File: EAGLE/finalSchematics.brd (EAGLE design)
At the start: 100 x 80 mm, 34 parts, among them IC1 STM32F103RBT, J2 U.FL, J3 U.FL, Q1 8MHz 131-220, U1 LM1117-3.3

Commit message: Death is near
Routing the board
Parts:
- added R1: 10k 901-655, rcl:R0805
- moved JP1 170.6 mm to (38.8, 4.67), flipped to the bottom, turned to 340 degrees
- moved LED3 167.3 mm to (49.5, 29.8), turned to 270 degrees
- moved 270OHM2 166.9 mm to (45.2, 29.8), turned to 180 degrees
- moved 270OHM1 158.5 mm to (45.2, 27.6), turned to 180 degrees
- moved LED2 158.3 mm to (49.5, 27.4), turned to 270 degrees
- moved 270OHM 156.5 mm to (45.3, 32.0), turned to 180 degrees
- moved D1 152.8 mm to (55.8, 39.5), flipped to the bottom, turned to 250 degrees
- moved LED1 151.4 mm to (49.6, 32.1), turned to 270 degrees
- moved J1 138.8 mm to (53.2, 34.8), turned to 180 degrees
- moved C7 120.0 mm to (21.6, 51.9), flipped to the bottom, turned to 270 degrees
- moved C3 111.1 mm to (33.6, 56.4), turned to 180 degrees
- moved C10 108.9 mm to (50.2, 21.6), turned to 270 degrees
- moved C11 102.3 mm to (30.0, 9.40), flipped to the bottom
- moved C8 94.1 mm to (9.14, 16.6), flipped to the bottom, turned to 180 degrees
- moved C9 89.1 mm to (35.3, 9.09), turned to 180 degrees
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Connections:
- removed net VBAT: IC1.1
- new net N$14: IC1.60, R1.2
- net +3V3: now also IC1.1
- net GND: now also R1.1
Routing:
- net GND: track 76.1 -> 205.8 mm, vias 2 -> 0
- net MOSI: track 0.00 -> 120.3 mm, vias 0 -> 2
- net 1PPS: track 0.00 -> 111.7 mm, vias 0 -> 1
- net SCK: track 0.00 -> 104.7 mm, vias 0 -> 2
- net MISO: track 0.00 -> 88.7 mm, vias 0 -> 2
- net CS-SD: track 0.00 -> 67.0 mm, vias 0 -> 2
- net SDA: track 87.2 -> 26.8 mm, vias 0 -> 2
- net SCL: track 82.9 -> 26.5 mm, vias 1 -> 0
- net DIO0: track 0.00 -> 48.6 mm, vias 0 -> 2
- net CS-RAD: track 0.00 -> 48.5 mm
- net RX: track 0.00 -> 42.1 mm, vias 0 -> 1
- net TX: track 0.00 -> 37.8 mm, vias 0 -> 1
- net SWDIO: track 0.00 -> 30.3 mm
- net N$3: track 0.00 -> 15.8 mm
- net +3V3: track 69.5 -> 84.3 mm, vias 2 -> 0
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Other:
- board size 100 x 80 mm -> 60 x 60 mm

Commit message: Finish Route PCB, prepare for inspection
Hakys je sport budoucnosti!
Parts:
- Q1: value 8MHz 131-220 -> (none); device crystal:HC49U-V -> crystal:HC49UP
- moved R1 8.37 mm to (24.1, 17.0)
- moved C2 6.16 mm to (47.1, 17.8), turned to 270 degrees
- moved Q1 4.21 mm to (50.6, 12.5), flipped to the bottom, turned to 310 degrees
- moved C1 0.96 mm to (43.3, 8.69)
- moved JP1 0.96 mm to (38.5, 3.76)
- moved R2 0.61 mm to (13.4, 9.65)
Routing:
- net +3V3: track 84.3 -> 228.0 mm, vias 0 -> 6
- net GND: track 205.8 -> 346.0 mm, vias 0 -> 7
- net N$1: track 0.00 -> 39.5 mm, vias 0 -> 1
- net N$8: track 0.00 -> 21.6 mm, vias 0 -> 2
- net N$2: track 0.00 -> 19.7 mm, vias 0 -> 1
- net N$14: track 4.94 -> 10.3 mm
- net SWDIO: track 30.3 -> 34.4 mm
- net TXDBG: track 13.5 -> 17.2 mm
- net CS-SD: track 67.0 -> 70.4 mm
- net MOSI: track 120.3 -> 117.5 mm
- net RX: track 42.1 -> 44.7 mm
- net TX: track 37.8 -> 39.8 mm
- net RXDBG: track 14.7 -> 16.0 mm
- net SWO: track 12.5 -> 13.6 mm
- net SCL: track 26.5 -> 25.9 mm
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
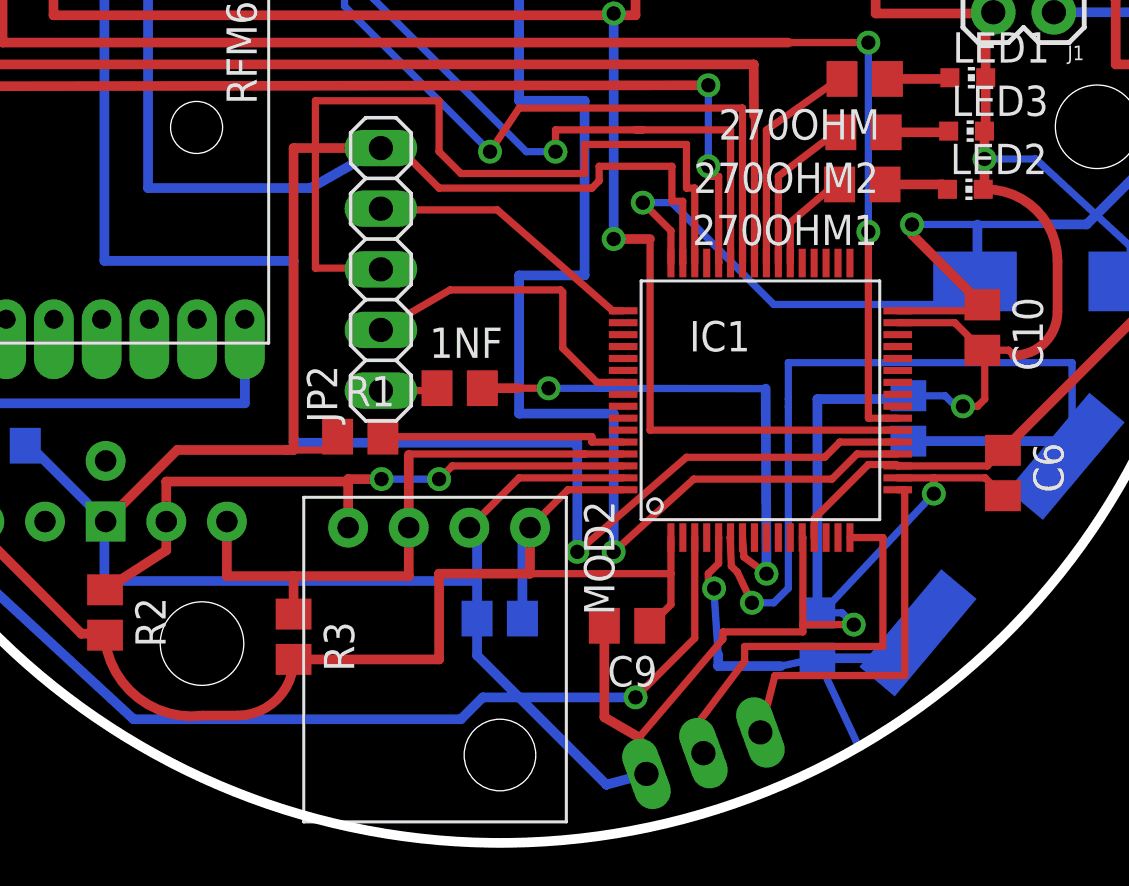
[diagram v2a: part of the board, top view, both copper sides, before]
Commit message: Fix route overlap
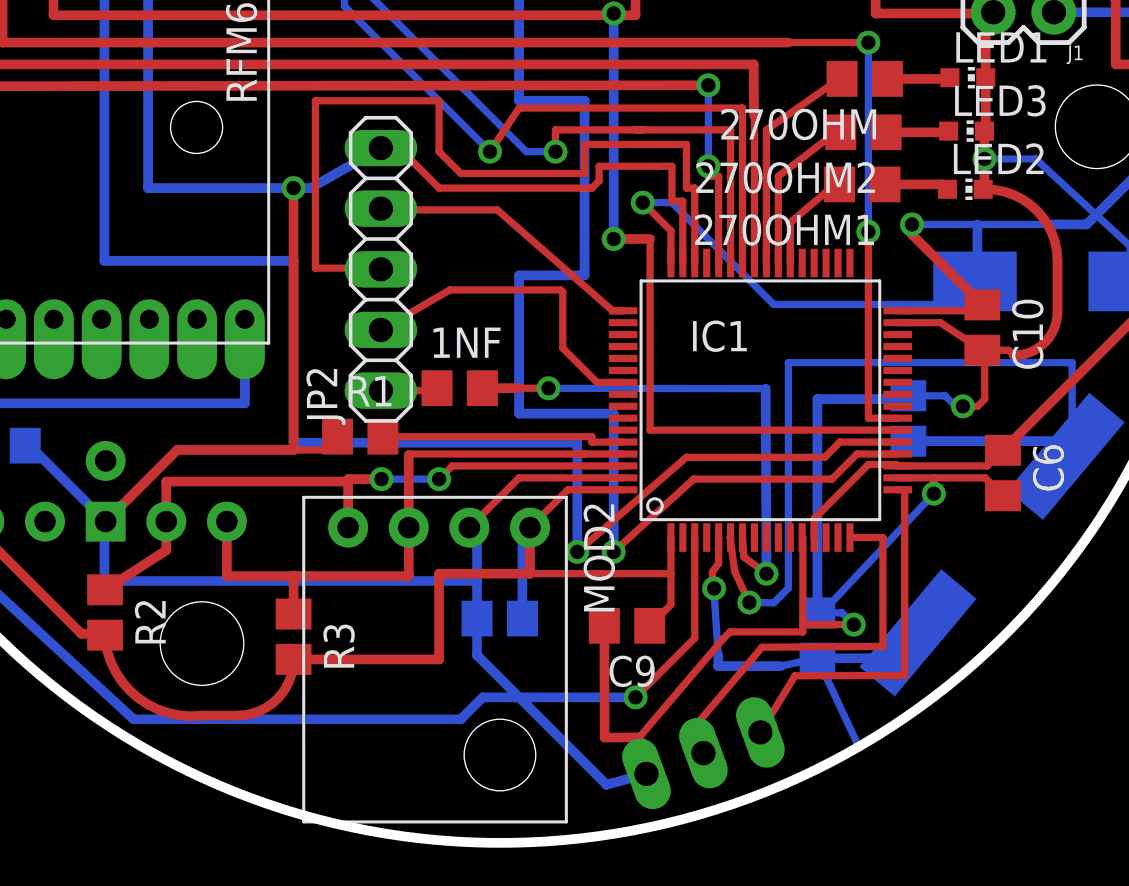
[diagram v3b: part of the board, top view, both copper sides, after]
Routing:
- net GND: track 346.0 -> 341.0 mm, vias 7 -> 8
- net RXDBG: track 16.0 -> 15.5 mm
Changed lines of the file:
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@@
 <wire x1="15.2936" y1="39.4372" x2="15.24" y2="39.4372" width="0.4064" layer="16"/>
 <wire x1="15.24" y1="39.4372" x2="15.24" y2="27.432" width="0.4064" layer="16"/>
-<wire x1="15.24" y1="27.432" x2="22.0472" y2="27.432" width="0.4064" layer="16"/>
+<wire x1="15.24" y1="27.432" x2="21.336" y2="27.432" width="0.4064" layer="16"/>
+<wire x1="21.336" y1="27.432" x2="22.0472" y2="27.432" width="0.4064" layer="16"/>
 <wire x1="22.0472" y1="27.432" x2="24.9936" y2="29.1084" width="0.4064" layer="16"/>
 <wire x1="41.805" y1="52.959" x2="41.7576" y2="52.959" width="0.4064" layer="16"/>
@@
 <wire x1="41.7576" y1="49.9872" x2="44.555" y2="49.9872" width="0.4064" layer="16"/>
 <wire x1="44.555" y1="49.9872" x2="44.555" y2="52.959" width="0.4064" layer="16"/>
-<wire x1="21.336" y1="29.1084" x2="24.9936" y2="29.1084" width="0.4064" layer="1"/>
-<wire x1="21.336" y1="29.1084" x2="21.336" y2="16.4592" width="0.4064" layer="1"/>
+<wire x1="21.336" y1="27.432" x2="21.336" y2="16.4592" width="0.4064" layer="1"/>
 <wire x1="21.336" y1="16.4592" x2="21.0312" y2="16.4592" width="0.4064" layer="1"/>
 <wire x1="21.0312" y1="16.4592" x2="16.4592" y2="16.4592" width="0.4064" layer="1"/>
 <wire x1="16.4592" y1="16.4592" x2="13.462" y2="13.462" width="0.4064" layer="1"/>
-<wire x1="34.356" y1="9.0932" x2="34.356" y2="5.26365" width="0.4064" layer="1"/>
-<wire x1="35.811825" y1="4.417425" x2="34.356" y2="5.26365" width="0.4064" layer="1"/>
+<wire x1="34.356" y1="9.0932" x2="34.366753125" y2="4.41426875" width="0.4064" layer="1"/>
+<wire x1="35.811825" y1="4.417425" x2="34.366753125" y2="4.41426875" width="0.4064" layer="1"/>
 <wire x1="35.811825" y1="4.417425" x2="36.11958125" y2="2.89046875" width="0.4064" layer="1"/>
 <wire x1="35.144" y1="15.292" x2="30.786" y2="15.292" width="0.3048" layer="1"/>
@@
 <wire x1="34.4424" y1="2.4384" x2="34.4483125" y2="2.4384" width="0.4064" layer="16"/>
 <wire x1="34.4483125" y1="2.4384" x2="36.11958125" y2="2.89046875" width="0.4064" layer="16"/>
-<wire x1="46.644" y1="21.792" x2="49.0384" y2="21.792" width="0.3048" layer="1"/>
-<wire x1="50.1904" y1="20.64" x2="49.0384" y2="21.792" width="0.3048" layer="1"/>
+<wire x1="46.644" y1="21.792" x2="48.4288" y2="21.792" width="0.3048" layer="1"/>
+<wire x1="50.1904" y1="20.64" x2="48.4288" y2="21.792" width="0.3048" layer="1"/>
 <wire x1="48.1584" y1="15.292" x2="46.644" y2="15.292" width="0.3048" layer="1"/>
 <wire x1="48.1584" y1="15.292" x2="50.306" y2="15.292" width="0.3048" layer="1"/>
@@
 <wire x1="42.672" y1="9.144" x2="42.672" y2="12.792" width="0.3048" layer="1"/>
 <wire x1="42.672" y1="9.144" x2="42.672" y2="8.8392" width="0.3048" layer="1"/>
-<wire x1="42.672" y1="8.8392" x2="39.3192" y2="8.8392" width="0.3048" layer="1"/>
+<wire x1="42.672" y1="8.8392" x2="39.624" y2="8.8392" width="0.3048" layer="1"/>
 <wire x1="39.3192" y1="8.5344" x2="35.811825" y2="4.417425" width="0.3048" layer="1"/>
-<wire x1="39.3192" y1="8.8392" x2="39.3192" y2="8.5344" width="0.3048" layer="1"/>
+<wire x1="39.624" y1="8.8392" x2="39.3192" y2="8.5344" width="0.3048" layer="1"/>
 <wire x1="50.1904" y1="20.64" x2="51.2928" y2="20.64" width="0.3048" layer="1"/>
 <wire x1="51.5112" y1="20.4216" x2="51.2928" y2="20.64" width="0.3048" layer="1"/>
@@
 <via x="29.66" y="45.1104" extent="1-16" drill="0.6"/>
 <wire x1="16.1256" y1="44.958" x2="18.8756" y2="44.958" width="0.4064" layer="16"/>
+<via x="21.336" y="27.432" extent="1-16" drill="0.6"/>
 </signal>
 <signal name="NC">
@@
 <contactref element="Q1" pad="1"/>
 <wire x1="39.644" y1="12.792" x2="39.624" y2="12.792" width="0.3048" layer="1"/>
-<wire x1="39.624" y1="12.792" x2="39.67606875" y2="11.594384375" width="0.3048" layer="1"/>
-<via x="40.5384" y="10.0584" extent="1-16" drill="0.6"/>
-<wire x1="39.67606875" y1="11.594384375" x2="39.9288" y2="11.341653125" width="0.3048" layer="1"/>
-<wire x1="39.9288" y1="11.341653125" x2="40.5384" y2="10.0584" width="0.3048" layer="1"/>
+<wire x1="39.624" y1="12.792" x2="39.80509375" y2="11.4438625" width="0.3048" layer="1"/>
+<via x="40.43088125" y="10.06915" extent="1-16" drill="0.6"/>
+<wire x1="39.80509375" y1="11.4438625" x2="39.82128125" y2="11.352403125" width="0.3048" layer="1"/>
+<wire x1="39.82128125" y1="11.352403125" x2="40.43088125" y2="10.06915" width="0.3048" layer="1"/>
 <wire x1="53.9496" y1="16.83" x2="47.0916" y2="16.83" width="0.4064" layer="16"/>
 <wire x1="54.2544" y1="16.83" x2="54.2544" y2="17.0688" width="0.4064" layer="16"/>
 <wire x1="54.2544" y1="17.0688" x2="54.2544" y2="17.3736" width="0.4064" layer="16"/>
-<wire x1="40.5384" y1="10.0584" x2="41.4528" y2="10.0584" width="0.3048" layer="16"/>
+<wire x1="40.43088125" y1="10.06915" x2="41.4528" y2="10.0584" width="0.3048" layer="16"/>
 <wire x1="41.4528" y1="10.0584" x2="42.0624" y2="10.668" width="0.3048" layer="16"/>
-<wire x1="42.0624" y1="10.668" x2="42.0624" y2="18.288" width="0.3048" layer="16"/>
-<wire x1="42.0624" y1="18.288" x2="42.0624" y2="18.5928" width="0.3048" layer="16"/>
-<wire x1="42.0624" y1="18.5928" x2="42.0624" y2="20.1168" width="0.3048" layer="16"/>
+<wire x1="42.0624" y1="10.668" x2="42.0624" y2="20.1168" width="0.3048" layer="16"/>
 <wire x1="42.0624" y1="20.1168" x2="53.9496" y2="20.1168" width="0.3048" layer="16"/>
 <wire x1="53.9496" y1="20.1168" x2="53.9496" y2="16.83" width="0.3048" layer="16"/>
@@
 <contactref element="Q1" pad="2"/>
 <wire x1="39.144" y1="12.792" x2="39.144" y2="11.712" width="0.3048" layer="1"/>
-<wire x1="38.7096" y1="11.2776" x2="38.7096" y2="10.903671875" width="0.3048" layer="1"/>
-<wire x1="38.7096" y1="10.903671875" x2="38.953615625" y2="10.65965625" width="0.3048" layer="1"/>
-<wire x1="39.144" y1="11.712" x2="38.7096" y2="11.2776" width="0.3048" layer="1"/>
+<wire x1="38.88163125" y1="11.3528625" x2="38.89238125" y2="10.914425" width="0.3048" layer="1"/>
+<wire x1="38.89238125" y1="10.914425" x2="38.953615625" y2="10.65965625" width="0.3048" layer="1"/>
+<wire x1="39.144" y1="11.712" x2="38.88163125" y2="11.3528625" width="0.3048" layer="1"/>
 <wire x1="41.7576" y1="7.406046875" x2="39.12478125" y2="7.406046875" width="0.4064" layer="16"/>
 <wire x1="39.12478125" y1="7.406046875" x2="39.12478125" y2="7.891484375" width="0.4064" layer="16"/>
@@
 <wire x1="36.855" y1="53.848" x2="36.8808" y2="53.848" width="0.4064" layer="1"/>
 <wire x1="36.8808" y1="58.2168" x2="36.8808" y2="53.848" width="0.4064" layer="1"/>
-<wire x1="22.86" y1="58.2168" x2="22.71846875" y2="58.120925" width="0" layer="19" extent="1-16"/>
 <wire x1="22.71846875" y1="58.120925" x2="13.4112" y2="51.816" width="0.4064" layer="1"/>
 <wire x1="13.2936" y1="39.4372" x2="13.4112" y2="39.4372" width="0.4064" layer="16"/>
@@
 <contactref element="JP1" pad="1"/>
 <wire x1="46.644" y1="14.792" x2="46.9392" y2="14.792" width="0.3048" layer="1"/>
-<wire x1="46.9392" y1="7.0104" x2="41.502821875" y2="7.0104" width="0.3048" layer="1"/>
-<wire x1="41.502821875" y1="7.0104" x2="40.893221875" y2="4.627928125" width="0.3048" layer="1"/>
+<wire x1="46.9392" y1="7.0104" x2="42.341478125" y2="6.99965" width="0.3048" layer="1"/>
+<wire x1="42.341478125" y1="6.99965" x2="40.893221875" y2="4.627928125" width="0.3048" layer="1"/>
 <wire x1="46.9392" y1="14.792" x2="46.9392" y2="7.0104" width="0.3048" layer="1"/>
 </signal>
@@
 <wire x1="44.644" y1="12.792" x2="46.0248" y2="12.792" width="0.3048" layer="1"/>
 <wire x1="46.0248" y1="12.792" x2="46.0248" y2="8.2296" width="0.3048" layer="1"/>
-<wire x1="46.0248" y1="8.2296" x2="40.2336" y2="8.2296" width="0.3048" layer="1"/>
-<wire x1="40.2336" y1="7.62" x2="38.4048" y2="5.1816" width="0.3048" layer="1"/>
+<wire x1="46.0248" y1="8.2296" x2="40.95773125" y2="8.19734375" width="0.3048" layer="1"/>
+<wire x1="40.427134375" y1="7.566240625" x2="38.4048" y2="5.1816" width="0.3048" layer="1"/>
 <wire x1="38.4048" y1="5.1816" x2="38.4048" y2="3.556" width="0.3048" layer="1"/>
 <wire x1="38.4048" y1="3.556" x2="38.5064" y2="3.7592" width="0.3048" layer="1"/>
-<wire x1="40.2336" y1="8.2296" x2="40.2336" y2="7.62" width="0.3048" layer="1"/>
+<wire x1="40.95773125" y1="8.19734375" x2="40.427134375" y2="7.566240625" width="0.3048" layer="1"/>
 </signal>
 <signal name="N$14">

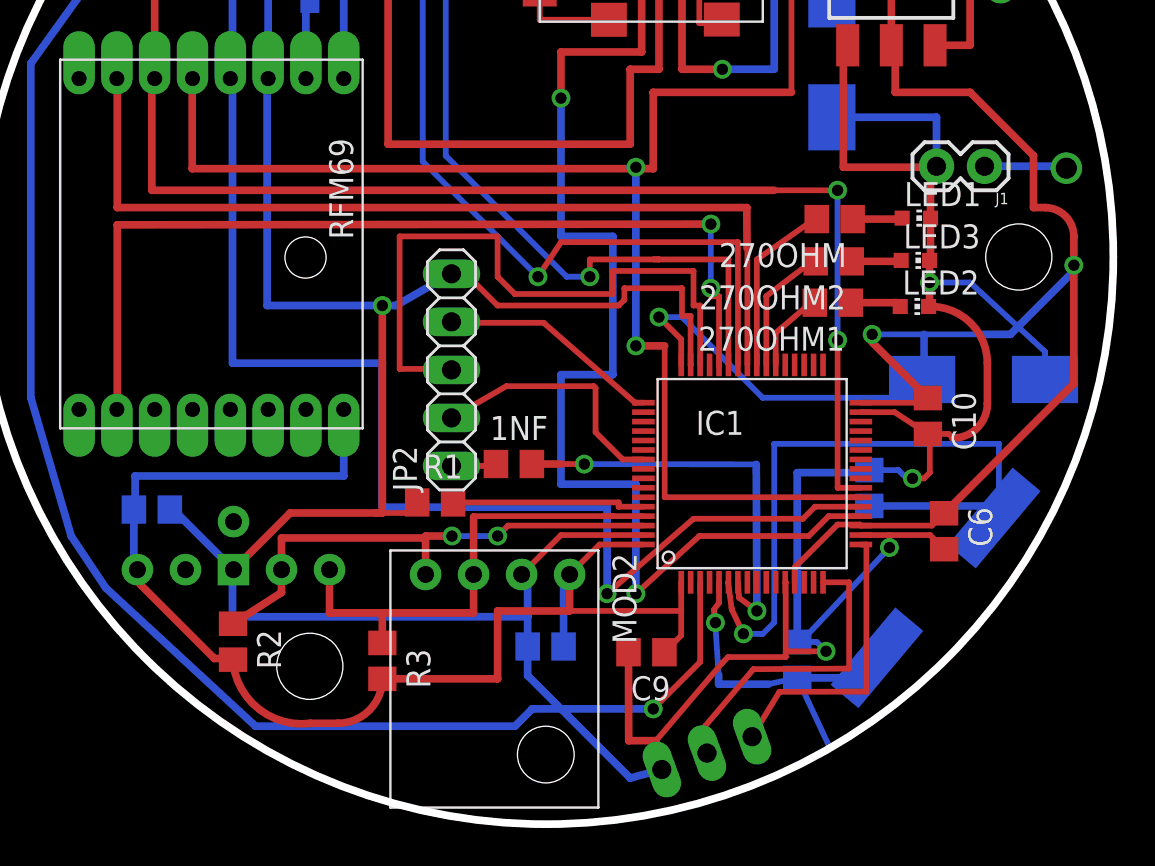
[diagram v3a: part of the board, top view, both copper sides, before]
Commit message: Small fix (overlap, clearance)
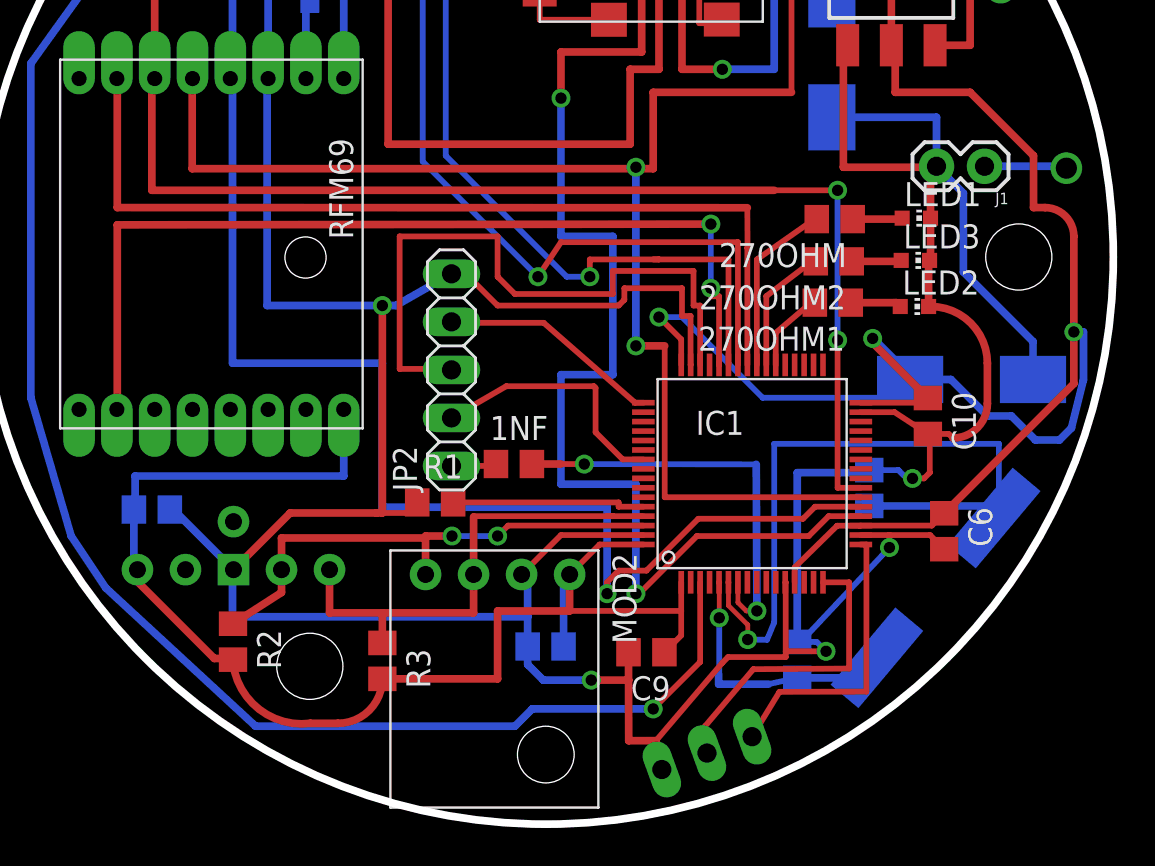
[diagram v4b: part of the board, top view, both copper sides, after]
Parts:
- moved C5 0.63 mm to (52.5, 23.5)
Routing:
- net N$2: track 19.5 -> 15.4 mm
- net +3V3: track 228.0 -> 229.4 mm
- net N$1: track 39.5 -> 40.2 mm
- net SCK: track 104.6 -> 105.2 mm

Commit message: Final fixes before etching
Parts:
- removed 1NF: (no value), rcl:C0805
- removed 270OHM, 270OHM1, 270OHM2: (no value), resistor:R0805
- added C12: 1n, rcl:C0805
- added R4, R5, R6: 270, resistor:R0805
- C1, C2: value 4.7p 906-099 -> 15p
- C10, C11, C3, C6, C7, C8, C9: value (none) -> 100n
- J1: value (none) -> PWR
- JP1: value (none) -> DBG
- JP2: value (none) -> SWD
- LED1, LED2, LED3: value (none) -> GRN
- Q1: value (none) -> 8 MHz
- SD1: value (none) -> SD
- moved J2 52.4 mm to (28.4, 2.67), flipped to the top
- moved R2 50.3 mm to (30.7, 56.9), turned to 180 degrees
- moved MOD3 47.6 mm to (43.2, 50.7), flipped to the top, turned to 270 degrees
- moved C6 47.2 mm to (21.3, 52.2)
- moved R3 47.0 mm to (30.7, 54.7), turned to 180 degrees
- moved JP1 46.1 mm to (18.2, 45.2), turned to 90 degrees
- moved MOD2 45.1 mm to (35.4, 57.7), turned to 180 degrees
- moved C11 44.5 mm to (37.7, 53.2), flipped to the top, turned to 180 degrees
- moved C1 42.1 mm to (25.0, 46.6), flipped to the top, turned to 0 degrees
- moved MOD4 41.7 mm to (36.2, 5.84), flipped to the top, turned to 90 degrees
- moved SD1 39.5 mm to (4.45, 29.6), flipped to the bottom, turned to 90 degrees
- moved Q1 39.2 mm to (29.9, 45.8), flipped to the top, turned to 90 degrees
- moved C2 34.6 mm to (24.9, 44.3), flipped to the top, turned to 0 degrees
- moved U1 33.5 mm to (44.3, 11.0), turned to 90 degrees
- moved J3 29.5 mm to (12.0, 16.0), turned to 90 degrees
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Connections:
- removed net N$4: D1.A, J1.1
- removed net N$8: 1NF.2, IC1.7
- net GND: now also C12.1, D1.A
- net N$10: now also R4.2; no longer 270OHM.2
- net N$11: now also R4.1; no longer 270OHM.1
- net N$12: now also R6.1; no longer 270OHM1.1
- net N$13: now also R5.1; no longer 270OHM2.1
- net N$3: now also J1.1
- net N$7: now also R6.2; no longer 270OHM1.2
- net N$9: now also R5.2; no longer 270OHM2.2
- net NRST: now also C12.2, IC1.7; no longer 1NF.1
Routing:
- net GND: track 341.0 -> 99.6 mm, vias 8 -> 16
- net +3V3: track 229.4 -> 42.4 mm, vias 6 -> 1
- net 1PPS: track 112.1 -> 26.5 mm, vias 1 -> 2
- net MOSI: track 117.5 -> 34.9 mm, vias 2 -> 0
- net SCK: track 105.2 -> 40.4 mm, vias 2 -> 0
- net MISO: track 89.1 -> 30.0 mm, vias 2 -> 0
- net CS-SD: track 70.5 -> 22.5 mm, vias 2 -> 1
- net RX: track 44.7 -> 9.36 mm, vias 1 -> 0
- net CS-RAD: track 48.5 -> 17.8 mm, vias 0 -> 1
- net TX: track 39.8 -> 9.76 mm, vias 1 -> 0
- net DIO0: track 49.2 -> 27.0 mm, vias 2 -> 1
- net N$8: track 21.9 -> 0.00 mm, vias 2 -> 0
- net SCL: track 25.9 -> 46.1 mm
- net NRST: track 2.45 -> 22.1 mm, vias 0 -> 1
- net N$1: track 40.2 -> 21.5 mm, vias 1 -> 0
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- added copper zone on layer 1, net +3V3
- added copper zone on layer 16, net GND
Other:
- board text added: "+"
- board text added: "2017"
- board text added: "Almighty Lobsters"
- board text added: "BOTTOM"
- board text added: "CanSat 1.0b"
- board text added: "GND TX RX"
- board text added: "MacGyver"
- board text added: "TOP"
- board text added: "bSTOP"
- board text added: "tSTOP"
